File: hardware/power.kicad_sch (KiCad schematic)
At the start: 34 parts, among them U2 LT3988, U3 RC4558

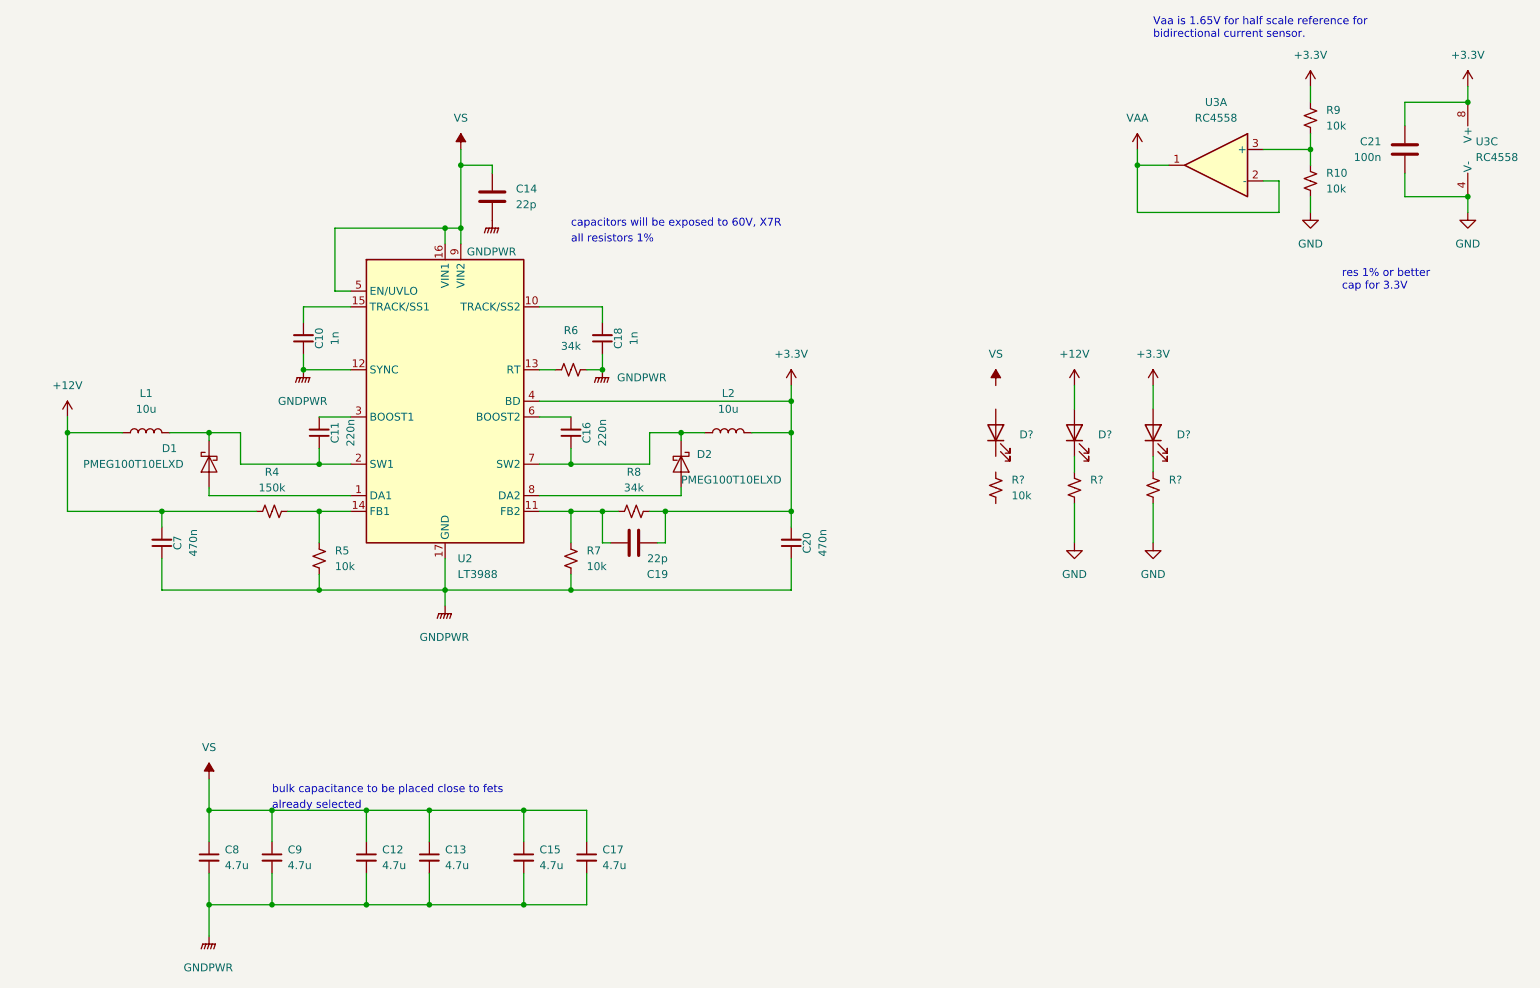
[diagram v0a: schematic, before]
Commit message: signal leds, bulk capacitance
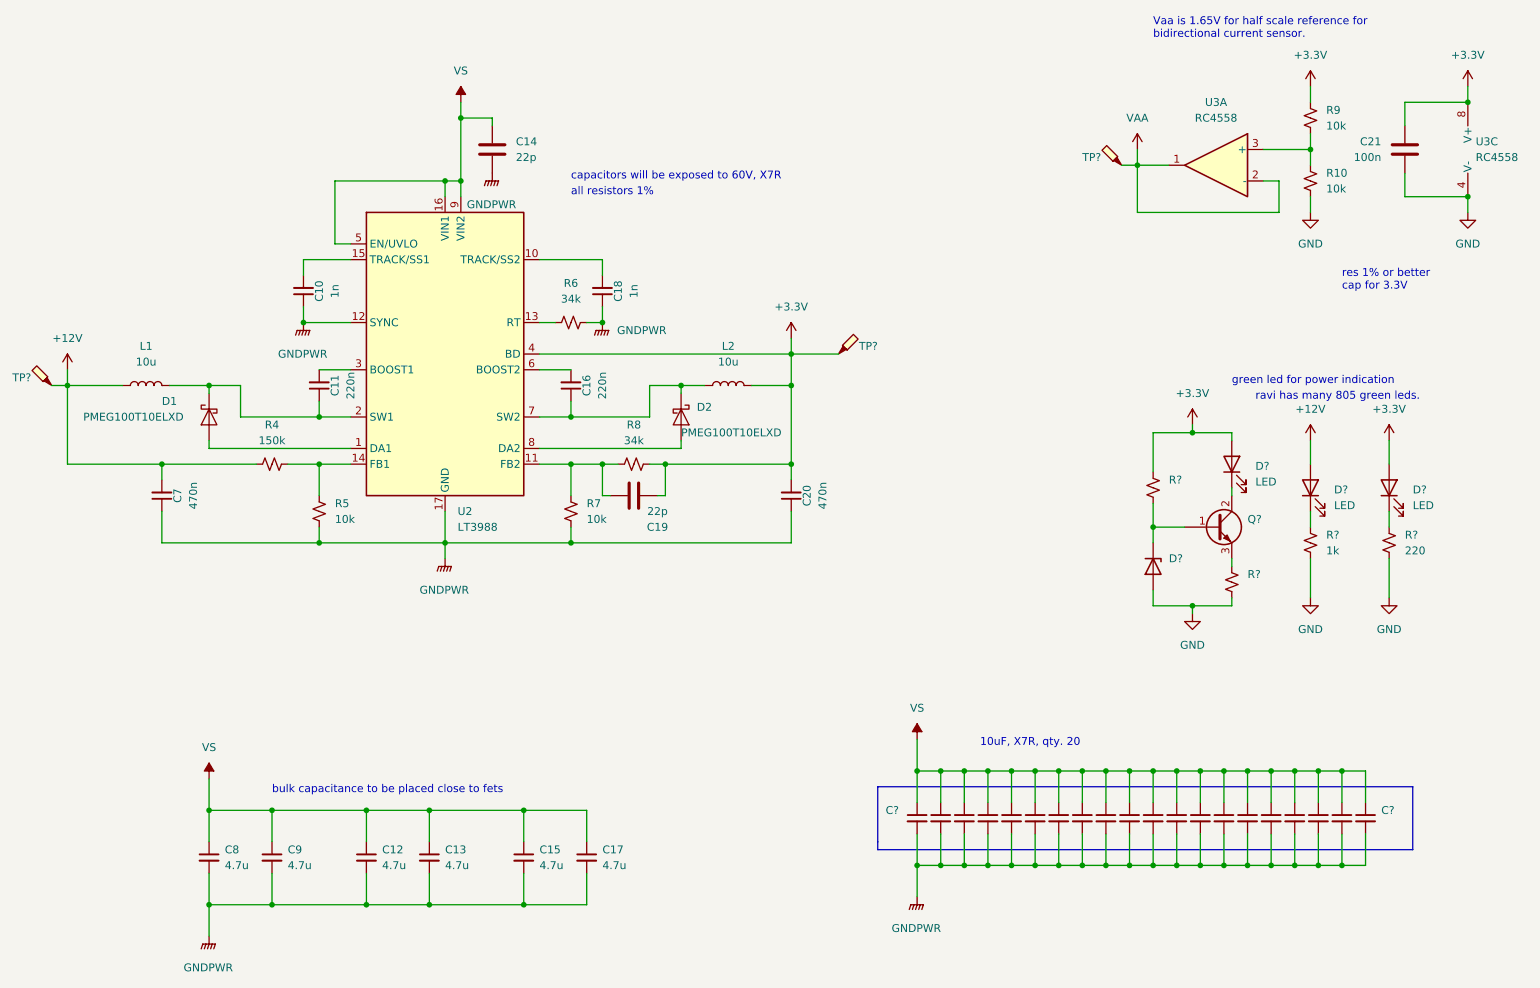
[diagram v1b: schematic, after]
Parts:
- removed D?: (no value), symbol Device:LED
- removed R?: 10k, Resistor_SMD:R_0805_2012Metric, symbol Device:R_Small_US
- added C? (x17): 10u, Capacitor_SMD:C_1210_3225Metric, symbol Device:C_Small
- added C? (x2): (no value), symbol Device:C_Small
- added C?: (no value), Capacitor_SMD:C_1210_3225Metric, symbol Device:C_Small
- added D?: (no value), symbol Device:D_Zener
- added D?: LED, symbol Device:LED
- added Q?: (no value), symbol Transistor_BJT:BCX56
- added R? (x2): (no value), Resistor_SMD:R_0805_2012Metric, symbol Device:R_Small_US
- added TP? (x2): TestPoint_Probe, symbol Connector:TestPoint_Probe
- added TP?: (no value), symbol Connector:TestPoint_Probe
- D? (x2): value (none) -> LED
- R?: value (none) -> 220
- R?: value (none) -> 1k
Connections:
- net +12V: now also TP?.1
- net +3V3: now also D?.2 (A), R?.1, TP?.1
- net GND: now also D?.2 (A), R?.2
- net GNDPWR: now also C?.2, C?.2, C?.2, C?.2, C?.2, C?.2, C?.2, C?.2, C?.2, C?.2, C?.2, C?.2, C?.2, C?.2, C?.2, C?.2, C?.2, C?.2, C?.2, C?.2
- net VAA: now also TP?.1
- net VS: now also C?.1, C?.1, C?.1, C?.1, C?.1, C?.1, C?.1, C?.1, C?.1, C?.1, C?.1, C?.1, C?.1, C?.1, C?.1, C?.1, C?.1, C?.1, C?.1, C?.1
- new net: Q?.3 (E), R?.1
- new net: D?.1 (K), Q?.1 (B), R?.2
- new net: D?.1 (K), Q?.2 (C)
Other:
- note added: "10uF, X7R, qty. 20"
- note added: "green led for power indication"
- note added: "ravi has many 805 green leds."
- note removed: "already selected"
- moved on the sheet: C10, C11, C14, C16, C18, C19, C20, C7, D1, D2, D?, L1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

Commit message: some layout
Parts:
- C21, C22, C40: renamed from C?; value (none) -> ~
- D3: renamed from D?; value (none) -> ~
- Q1: renamed from Q?; value (none) -> ~
- R10, R9: renamed from R?; value (none) -> ~
- TP1: renamed from TP?; value (none) -> ~
- gave numbers to parts that had none: 24
- renumbered C21 to C41, R9 to R11, R10 to R12

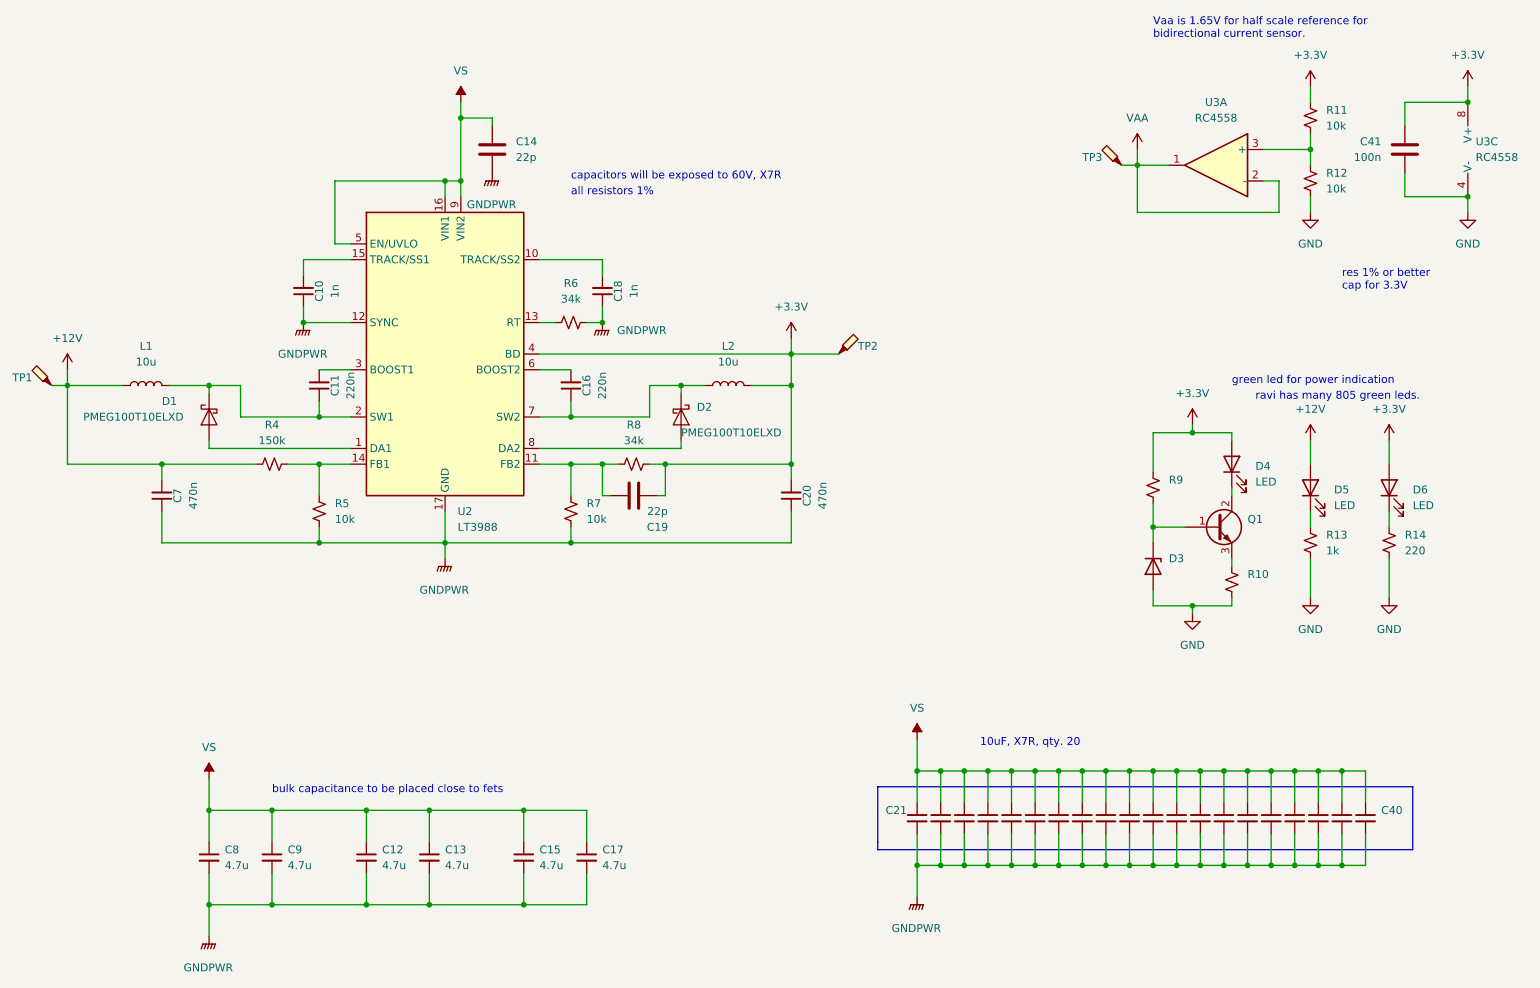
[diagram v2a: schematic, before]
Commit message: Simplified sensing, added some power layout.
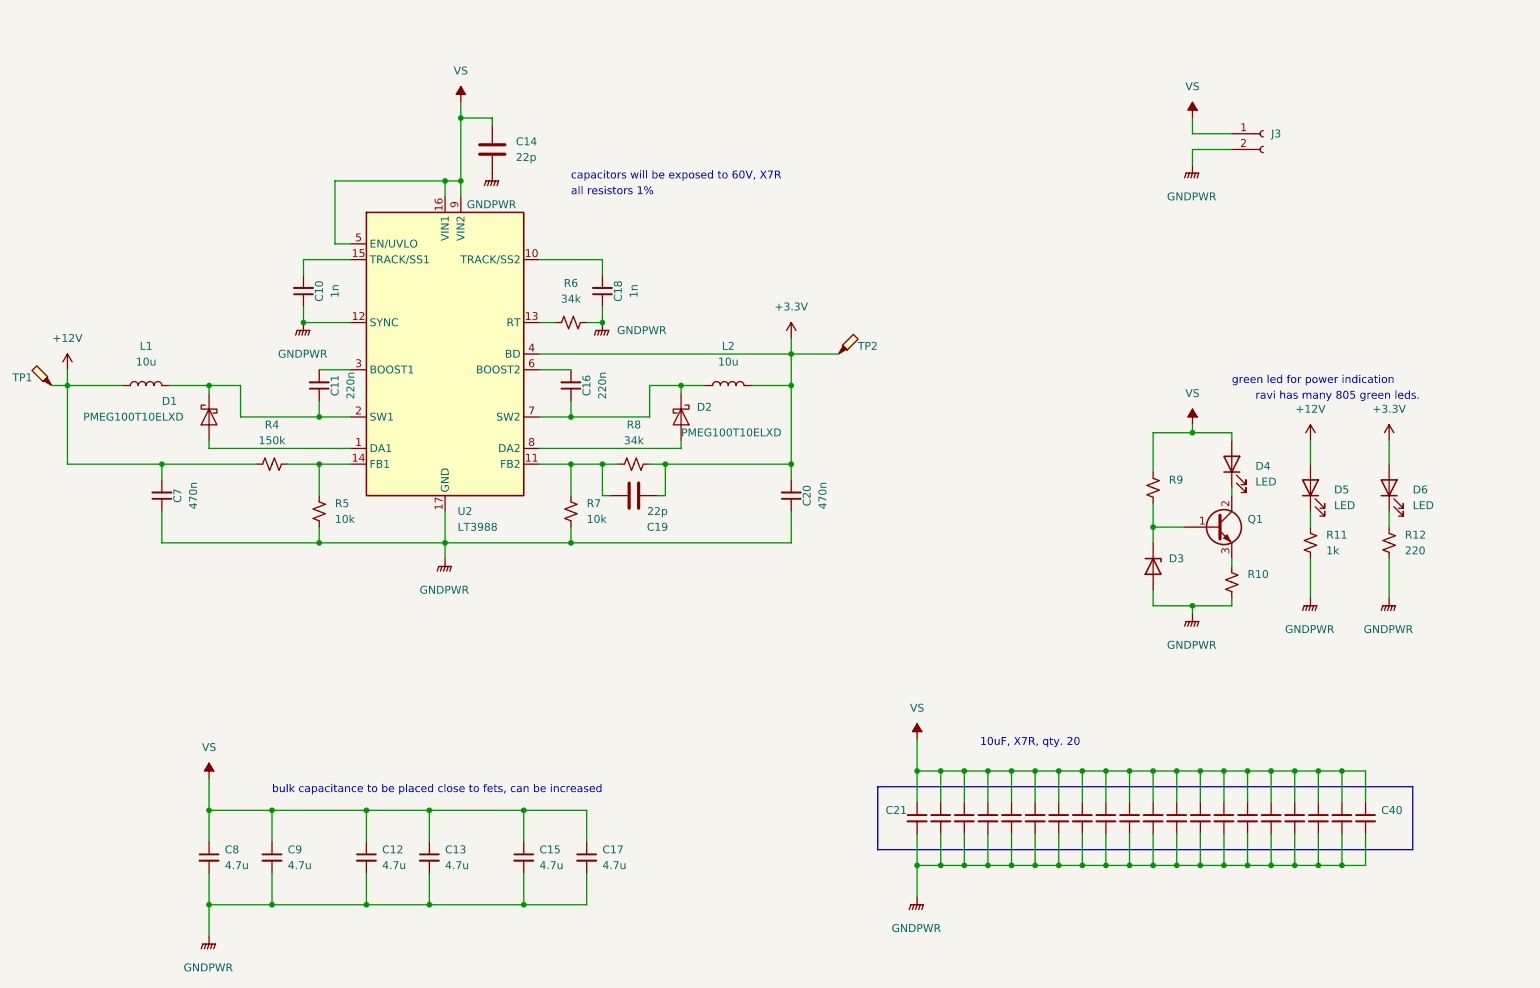
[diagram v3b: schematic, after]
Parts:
- removed C41: 100n, Capacitor_SMD:C_0402_1005Metric, symbol Device:C
- removed R11, R12: 10k, Resistor_SMD:R_0805_2012Metric, symbol Device:R_Small_US
- removed TP3: TestPoint_Probe, symbol Connector:TestPoint_Probe
- removed U3: RC4558, Package_SO:SOIC-8-1EP_3.9x4.9mm_P1.27mm_EP2.514x3.2mm, symbol Amplifier_Operational:RC4558
- added J3: (no value), symbol Connector:Conn_01x02_Female
- C21, C40: footprint (none) -> Capacitor_SMD:C_1210_3225Metric
- D3: footprint (none) -> Diode_SMD:D_SOD-523; Mouser (none) -> https://www.mouser.com/ProductDetail/Comchip-Technology/CZR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
- D4, D5, D6: footprint (none) -> LED_SMD:LED_0805_2012Metric
- Q1: footprint (none) -> Package_TO_SOT_SMD:SOT-89-3
- renumbered R13 to R11, R14 to R12
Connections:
- net GND is gone; now on net GNDPWR: D3.2 (A), R10.2, R11.2, R12.2
- net +3V3: no longer D4.2 (A), R9.1
- net GNDPWR: now also J3.2 (Pin_2)
- net VS: now also D4.2 (A), R9.1, J3.1 (Pin_1)
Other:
- note added: "bulk capacitance to be placed close to fets, can be increased"
- note removed: "Vaa is 1.65V for half scale reference for bidirectional current sensor."
- note removed: "bulk capacitance to be placed close to fets"
- note removed: "res 1% or better cap for 3.3V"
